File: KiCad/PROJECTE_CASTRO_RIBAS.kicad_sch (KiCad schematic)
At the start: 0 parts

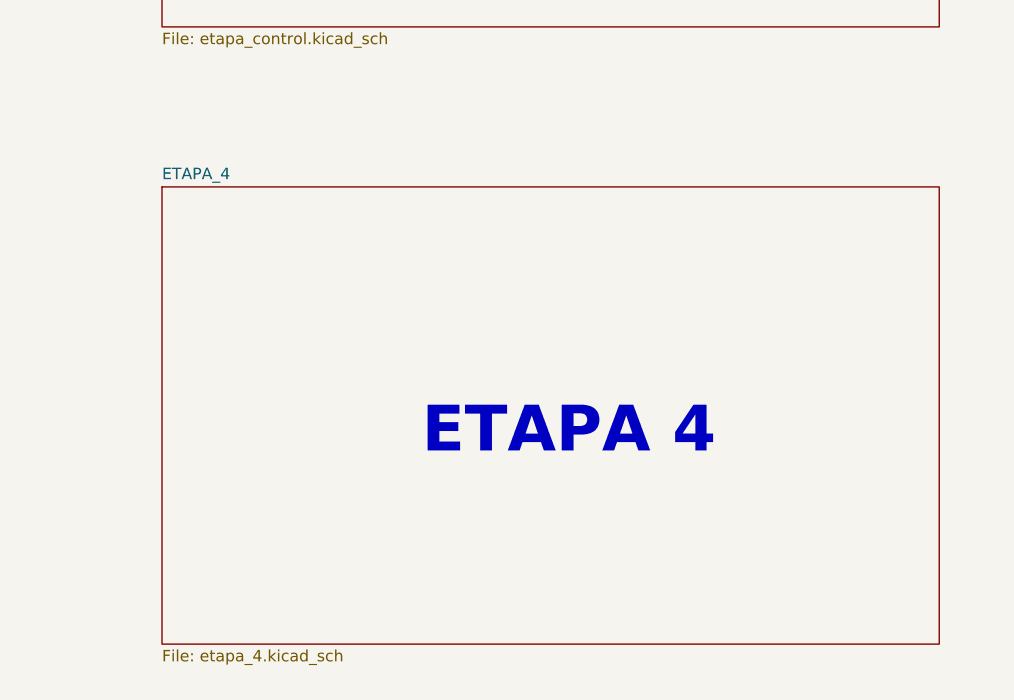
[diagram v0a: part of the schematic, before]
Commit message: TOTS ELS NOMS DE LES ETAPES JA POSATS
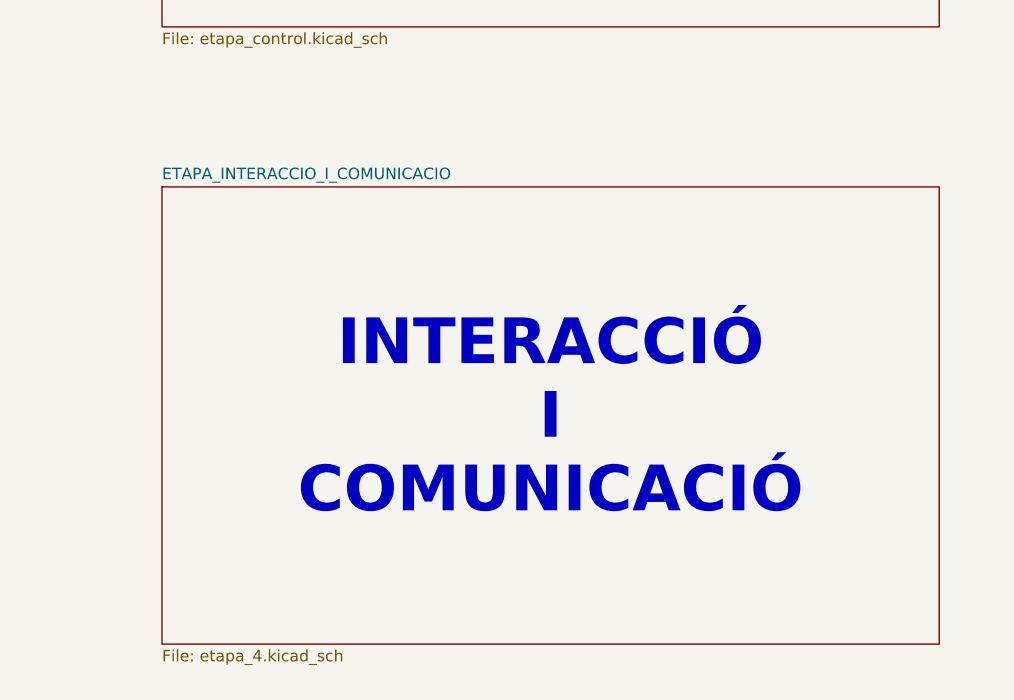
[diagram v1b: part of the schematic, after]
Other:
- sheet ETAPA_4 renamed ETAPA_INTERACCIO_I_COMUNICACIO
- note added: "INTERACCIÓ I COMUNICACIÓ"
- note removed: "ETAPA 4"
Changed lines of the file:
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@@
 		)
 	)
-	(text "ETAPA 4"
+	(text "INTERACCIÓ\nI\nCOMUNICACIÓ"
 		(exclude_from_sim no)
-		(at 191.262 122.428 0)
+		(at 189.23 120.904 0)
 		(effects
 			(font
@@
 			(color 0 0 0 0.0000)
 		)
-		(property "Sheetname" "ETAPA_4"
+		(property "Sheetname" "ETAPA_INTERACCIO_I_COMUNICACIO"
 			(at 146.05 94.5384 0)
 			(effects

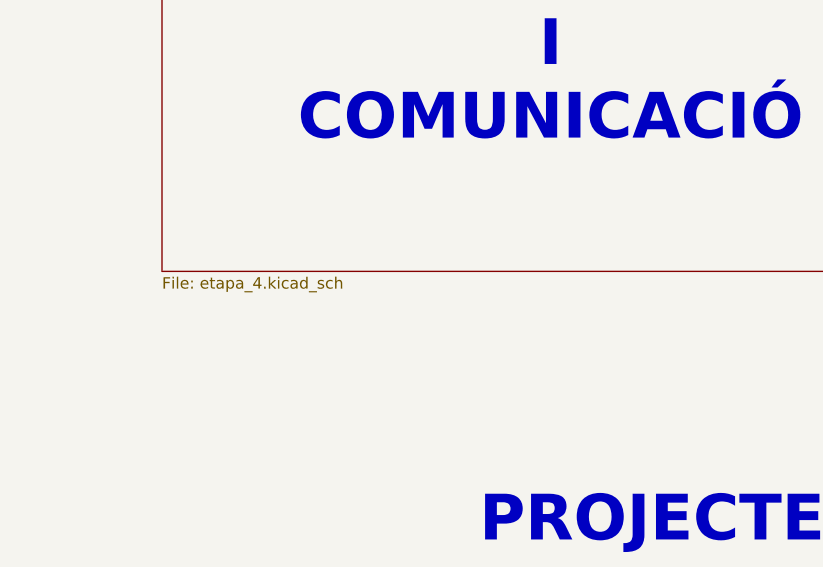
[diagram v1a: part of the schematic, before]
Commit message: Guardem completament la interacció i canvis de control
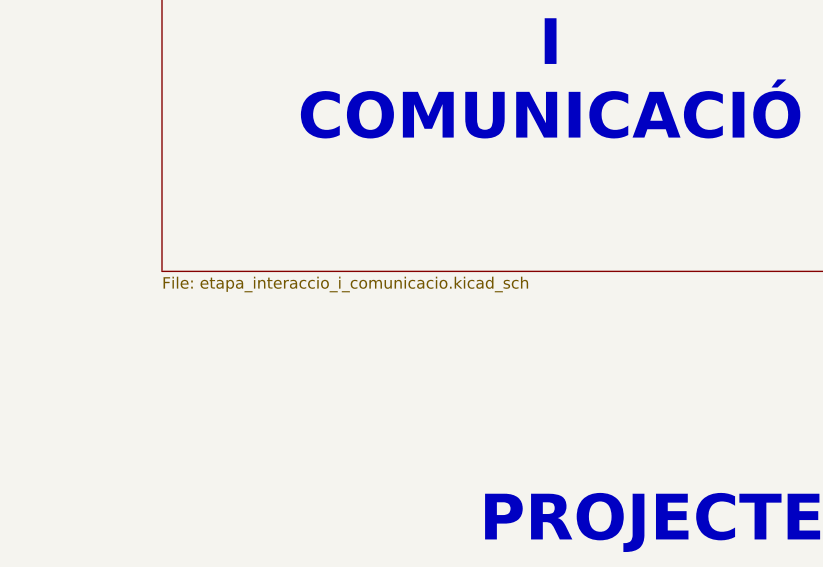
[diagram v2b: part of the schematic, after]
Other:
- sheet ETAPA_INTERACCIO_I_COMUNICACIO: file etapa_4.kicad_sch -> etapa_interaccio_i_comunicacio.kicad_sch
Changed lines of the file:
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@@
 			)
 		)
-		(property "Sheetfile" "etapa_4.kicad_sch"
+		(property "Sheetfile" "etapa_interaccio_i_comunicacio.kicad_sch"
 			(at 146.05 146.6346 0)
 			(effects
